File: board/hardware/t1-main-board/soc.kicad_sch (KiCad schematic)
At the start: 0 parts

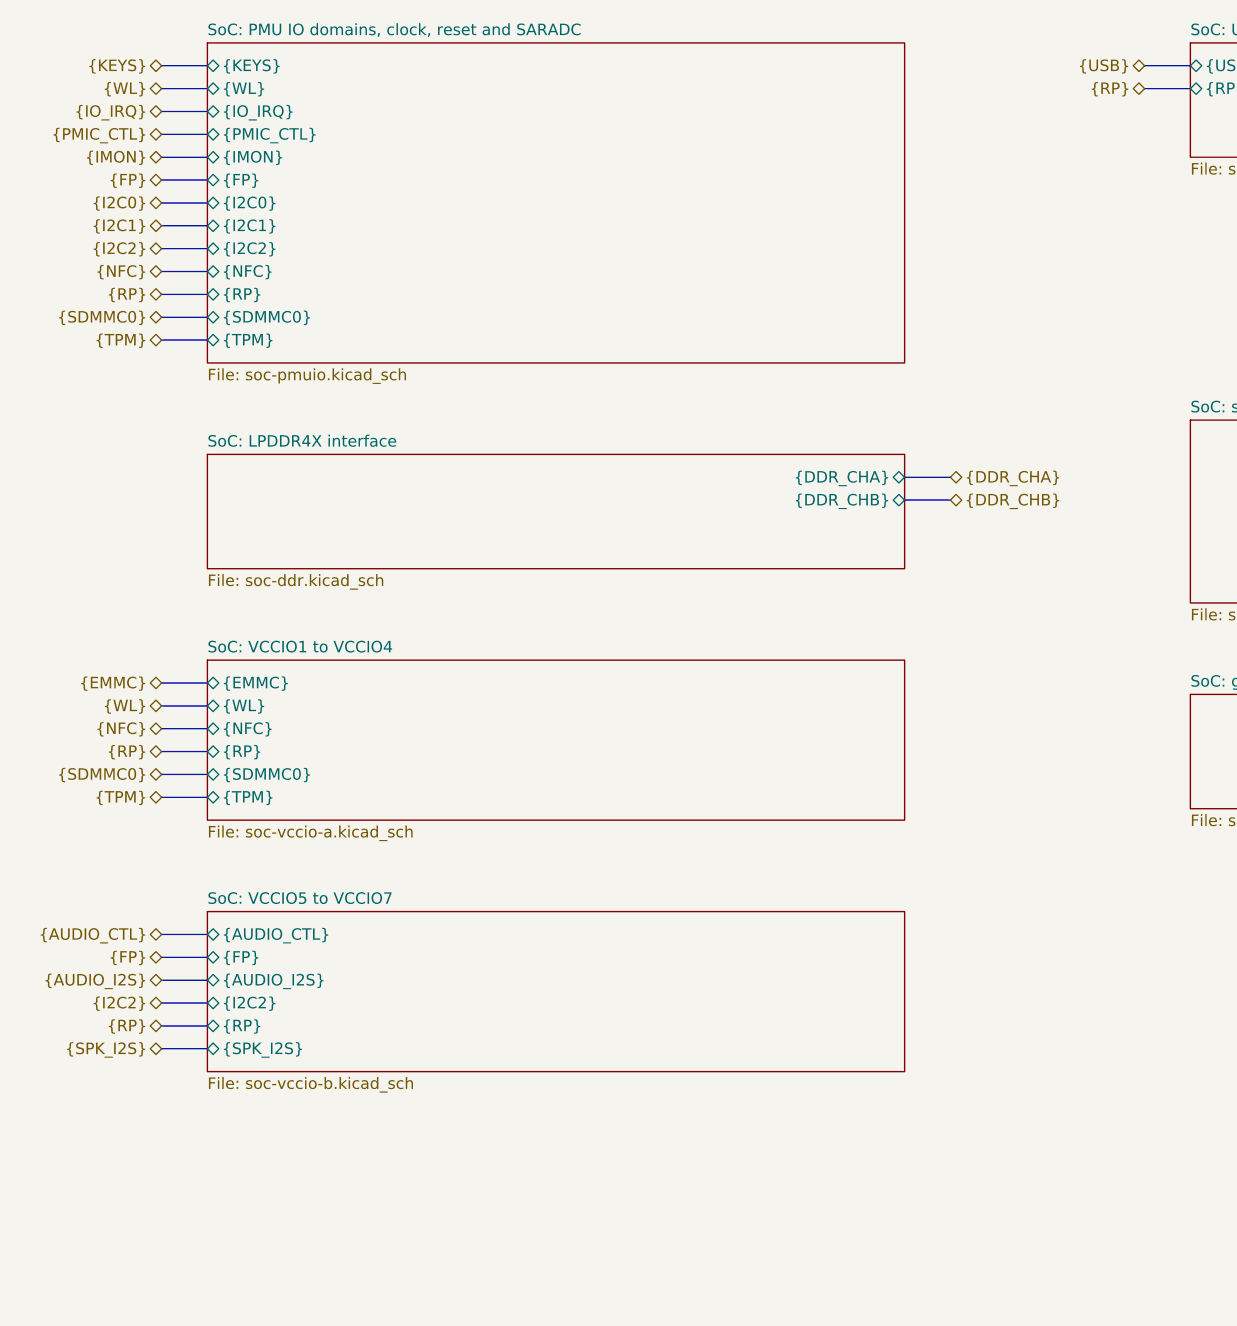
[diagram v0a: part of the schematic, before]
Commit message: Board: capture blk.debug
Debug UART2 (1.8 V) and I2S/DSD pads with ground pads, reset, PMIC and
power-key pads (PCB-T-09), a pad on every spare SoC GPIO whose pinout v1
row names one (the DEBUG bus, on the SoC's right edge), and a rail pad
for each power-tree rail no other sheet probes (PCB-T-02). Each DAC
sheet carries a pad on its MCLK. The spares pinout v1 leaves without a
pad now carry no-connect flags. On the root, facing sheet pins are
joined directly only where the route meets no other symbol.

Co-Authored-By: Claude Opus 5.5 <noreply@anthropic.com>
Claude-Session: https://claude.ai/code/session_01Ei262h3TpgY9vyfNLMi5Mn
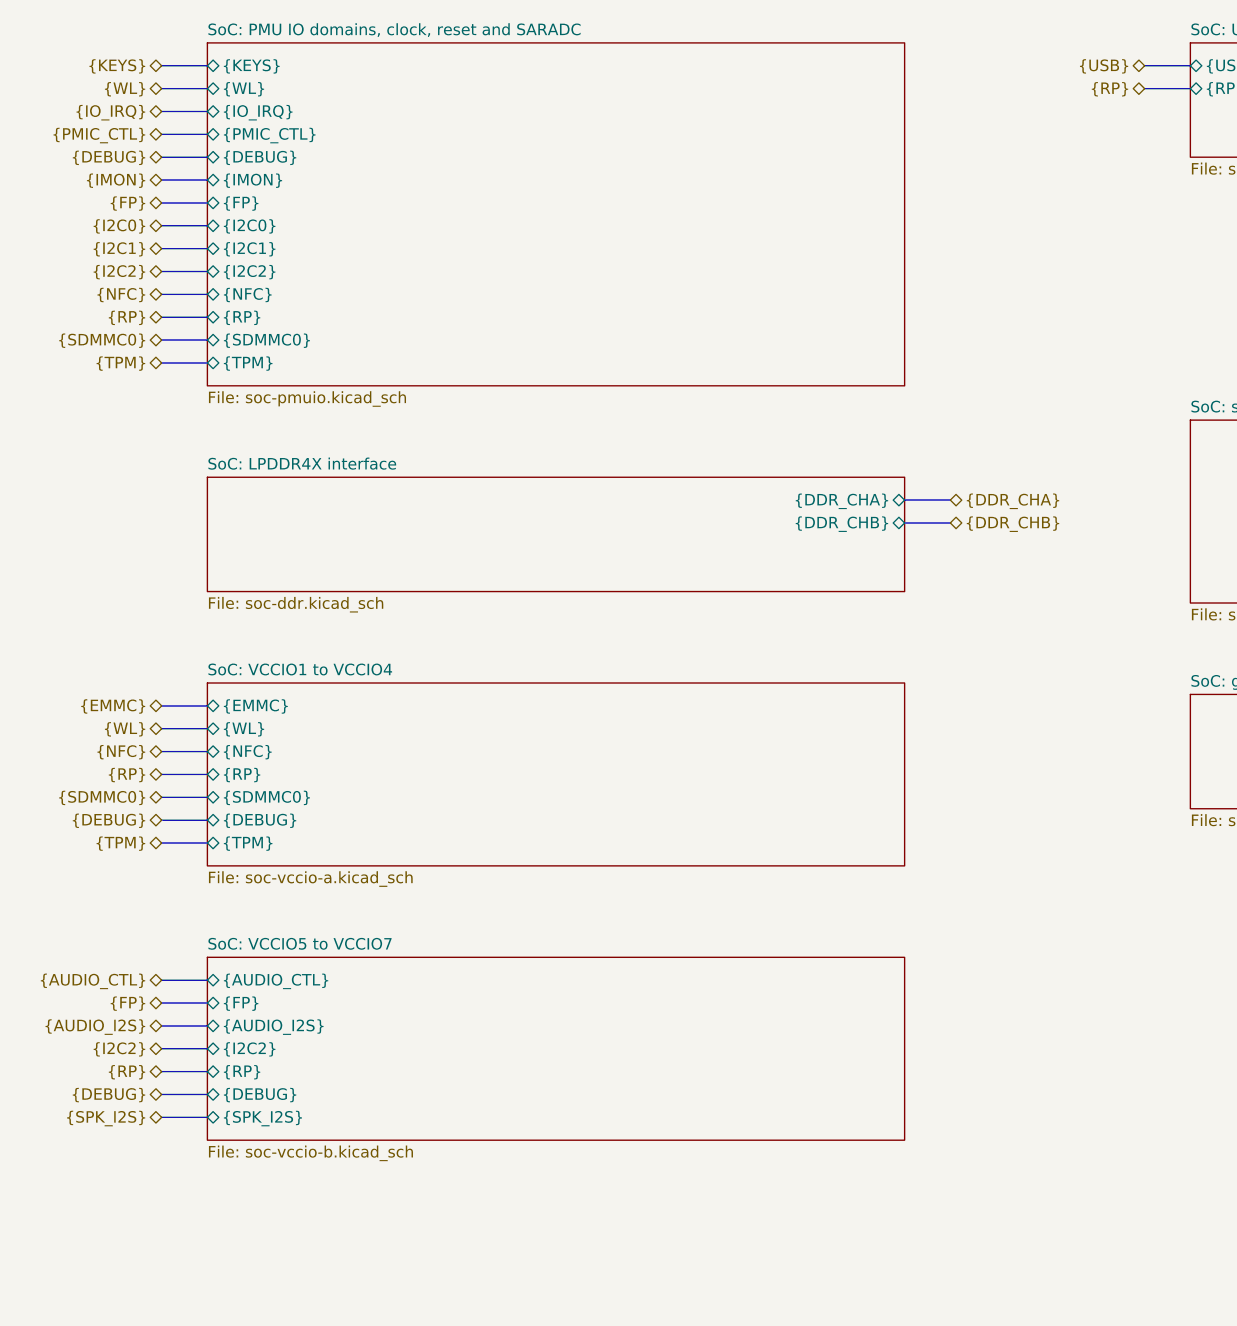
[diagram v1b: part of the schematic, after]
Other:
- sheet SoC: PMU IO domains, clock, reset and SARADC ports: added {DEBUG}; removed none
- sheet SoC: VCCIO1 to VCCIO4 ports: added {DEBUG}; removed none
- sheet SoC: VCCIO5 to VCCIO7 ports: added {DEBUG}; removed none

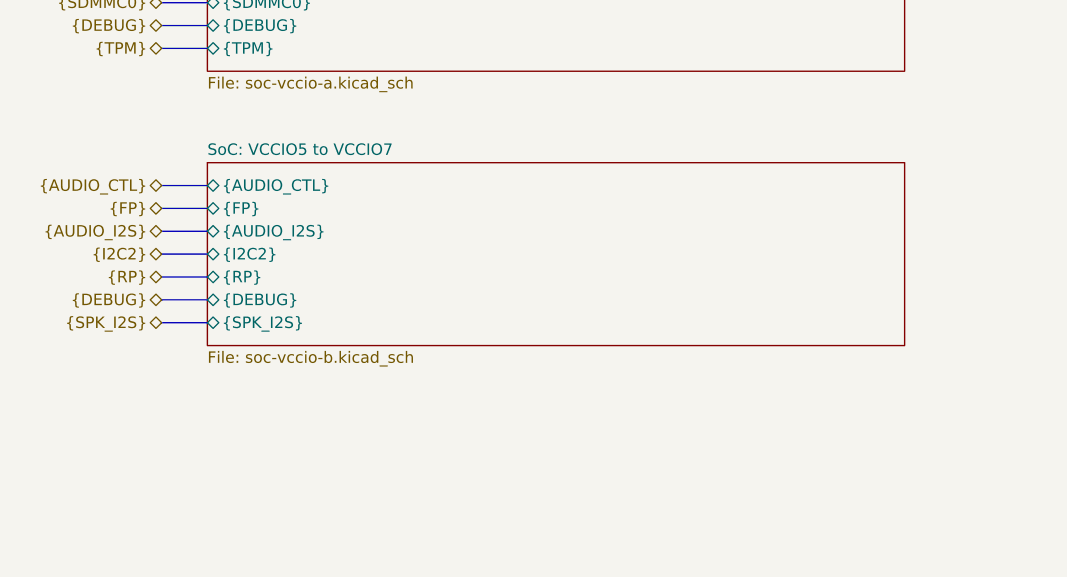
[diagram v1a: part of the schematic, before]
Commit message: Board: capture blk.mic-ambient and links #34, #35
IM73D122 on PDM CLK1 and SDI1 (BOM v1 line 34, pinout v1 AK2 and 1P2),
LR to ground, 22 Ω clock series, VDD from MIC_1V8 through link #35.
Link #34 on blk.mic-main makes the faceplate branch the rail MIC_1V8_FP
for contact 40 (power tree §4.12, G10). kicad-lib moves to e46bda4 for
the IM73D122, TPS3808G01, SN74LVC1G58 and BAT54 parts.

Co-Authored-By: Claude Opus 5.5 <noreply@anthropic.com>
Claude-Session: https://claude.ai/code/session_01Ei262h3TpgY9vyfNLMi5Mn
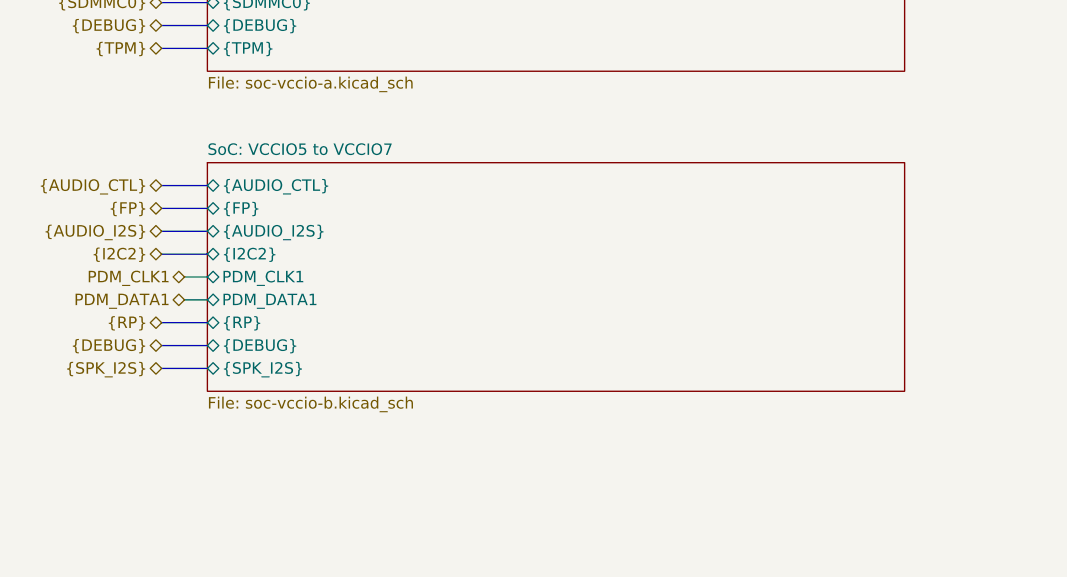
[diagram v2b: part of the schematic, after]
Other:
- sheet SoC: VCCIO5 to VCCIO7 ports: added PDM_CLK1, PDM_DATA1; removed none
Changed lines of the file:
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@@
   (instances (project "t1-main-board" (path "/7746052e-d7f9-59ad-ba73-bd2b74439529/8302eaa7-1fc9-5a34-8a84-8a9171d22bdf" (page "16"))))
 )
-(sheet (at 41.91 132.08) (size 77.47 20.32) (exclude_from_sim no) (in_bom yes) (on_board yes) (dnp no) (fields_autoplaced yes) (stroke (width 0.1524) (type solid)) (fill (color 0 0 0 0.0000))
+(sheet (at 41.91 132.08) (size 77.47 25.4) (exclude_from_sim no) (in_bom yes) (on_board yes) (dnp no) (fields_autoplaced yes) (stroke (width 0.1524) (type solid)) (fill (color 0 0 0 0.0000))
   (property "Sheetname" "SoC: VCCIO5 to VCCIO7" (at 41.91 131.368 0) (effects (font (size 1.27 1.27)) (justify left bottom)))
-  (property "Sheetfile" "soc-vccio-b.kicad_sch" (at 41.91 152.988 0) (effects (font (size 1.27 1.27)) (justify left top)))
-  (property "Block" "blk.soc-vccio-b" (at 41.91 155.528 0) (effects (font (size 1.27 1.27)) (justify left top)) (hide yes))
+  (property "Sheetfile" "soc-vccio-b.kicad_sch" (at 41.91 158.068 0) (effects (font (size 1.27 1.27)) (justify left top)))
+  (property "Block" "blk.soc-vccio-b" (at 41.91 160.608 0) (effects (font (size 1.27 1.27)) (justify left top)) (hide yes))
   (pin "{AUDIO_CTL}" bidirectional (at 41.91 134.62 180) (effects (font (size 1.27 1.27)) (justify left)))
   (pin "{FP}" bidirectional (at 41.91 137.16 180) (effects (font (size 1.27 1.27)) (justify left)))
   (pin "{AUDIO_I2S}" bidirectional (at 41.91 139.7 180) (effects (font (size 1.27 1.27)) (justify left)))
   (pin "{I2C2}" bidirectional (at 41.91 142.24 180) (effects (font (size 1.27 1.27)) (justify left)))
-  (pin "{RP}" bidirectional (at 41.91 144.78 180) (effects (font (size 1.27 1.27)) (justify left)))
-  (pin "{DEBUG}" bidirectional (at 41.91 147.32 180) (effects (font (size 1.27 1.27)) (justify left)))
-  (pin "{SPK_I2S}" bidirectional (at 41.91 149.86 180) (effects (font (size 1.27 1.27)) (justify left)))
+  (pin "PDM_CLK1" bidirectional (at 41.91 144.78 180) (effects (font (size 1.27 1.27)) (justify left)))
+  (pin "PDM_DATA1" bidirectional (at 41.91 147.32 180) (effects (font (size 1.27 1.27)) (justify left)))
+  (pin "{RP}" bidirectional (at 41.91 149.86 180) (effects (font (size 1.27 1.27)) (justify left)))
+  (pin "{DEBUG}" bidirectional (at 41.91 152.4 180) (effects (font (size 1.27 1.27)) (justify left)))
+  (pin "{SPK_I2S}" bidirectional (at 41.91 154.94 180) (effects (font (size 1.27 1.27)) (justify left)))
   (instances (project "t1-main-board" (path "/7746052e-d7f9-59ad-ba73-bd2b74439529/8302eaa7-1fc9-5a34-8a84-8a9171d22bdf" (page "17"))))
 )
@@
 (bus (pts (xy 41.91 116.84) (xy 36.83 116.84)) (stroke (width 0) (type default)))
 (hierarchical_label "{DEBUG}" (shape bidirectional) (at 36.83 116.84 180) (effects (font (size 1.27 1.27)) (justify right)))
-(bus (pts (xy 41.91 147.32) (xy 36.83 147.32)) (stroke (width 0) (type default)))
-(hierarchical_label "{DEBUG}" (shape bidirectional) (at 36.83 147.32 180) (effects (font (size 1.27 1.27)) (justify right)))
+(bus (pts (xy 41.91 152.4) (xy 36.83 152.4)) (stroke (width 0) (type default)))
+(hierarchical_label "{DEBUG}" (shape bidirectional) (at 36.83 152.4 180) (effects (font (size 1.27 1.27)) (justify right)))
 (bus (pts (xy 41.91 45.72) (xy 36.83 45.72)) (stroke (width 0) (type default)))
 (hierarchical_label "{IMON}" (shape bidirectional) (at 36.83 45.72 180) (effects (font (size 1.27 1.27)) (justify right)))
@@
 (bus (pts (xy 41.91 111.76) (xy 36.83 111.76)) (stroke (width 0) (type default)))
 (hierarchical_label "{RP}" (shape bidirectional) (at 36.83 111.76 180) (effects (font (size 1.27 1.27)) (justify right)))
-(bus (pts (xy 41.91 144.78) (xy 36.83 144.78)) (stroke (width 0) (type default)))
-(hierarchical_label "{RP}" (shape bidirectional) (at 36.83 144.78 180) (effects (font (size 1.27 1.27)) (justify right)))
+(bus (pts (xy 41.91 149.86) (xy 36.83 149.86)) (stroke (width 0) (type default)))
+(hierarchical_label "{RP}" (shape bidirectional) (at 36.83 149.86 180) (effects (font (size 1.27 1.27)) (justify right)))
 (bus (pts (xy 151.13 35.56) (xy 146.05 35.56)) (stroke (width 0) (type default)))
 (hierarchical_label "{RP}" (shape bidirectional) (at 146.05 35.56 180) (effects (font (size 1.27 1.27)) (justify right)))
@@
 (bus (pts (xy 41.91 139.7) (xy 36.83 139.7)) (stroke (width 0) (type default)))
 (hierarchical_label "{AUDIO_I2S}" (shape bidirectional) (at 36.83 139.7 180) (effects (font (size 1.27 1.27)) (justify right)))
-(bus (pts (xy 41.91 149.86) (xy 36.83 149.86)) (stroke (width 0) (type default)))
-(hierarchical_label "{SPK_I2S}" (shape bidirectional) (at 36.83 149.86 180) (effects (font (size 1.27 1.27)) (justify right)))
+(wire (pts (xy 41.91 144.78) (xy 39.37 144.78)) (stroke (width 0) (type default)))
+(hierarchical_label "PDM_CLK1" (shape bidirectional) (at 39.37 144.78 180) (effects (font (size 1.27 1.27)) (justify right)))
+(wire (pts (xy 41.91 147.32) (xy 39.37 147.32)) (stroke (width 0) (type default)))
+(hierarchical_label "PDM_DATA1" (shape bidirectional) (at 39.37 147.32 180) (effects (font (size 1.27 1.27)) (justify right)))
+(bus (pts (xy 41.91 154.94) (xy 36.83 154.94)) (stroke (width 0) (type default)))
+(hierarchical_label "{SPK_I2S}" (shape bidirectional) (at 36.83 154.94 180) (effects (font (size 1.27 1.27)) (justify right)))
 (bus (pts (xy 151.13 33.02) (xy 146.05 33.02)) (stroke (width 0) (type default)))
 (hierarchical_label "{USB}" (shape bidirectional) (at 146.05 33.02 180) (effects (font (size 1.27 1.27)) (justify right)))

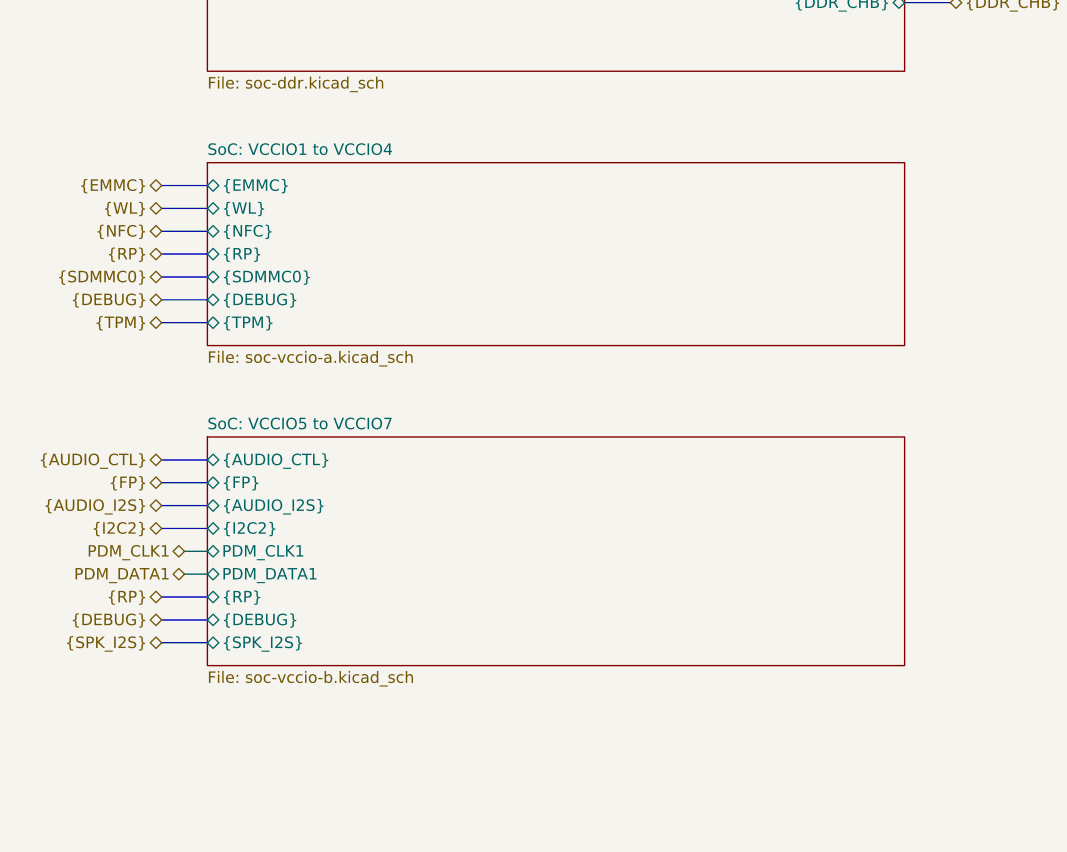
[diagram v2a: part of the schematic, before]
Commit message: NFC reader withdrawn from the board, every model (BRD-057)
Maintainer decision 2026-10-27, reason: board area. blk.nfc-reader (#42)
withdrawn: PN7160, front end, crystal, antenna contacts, NFC_VBAT switch
and link #18 removed (35 parts). BRD-057 reworded: NFC as the dynamic tag
only; blk.nfc-tag stays. Pinout v1: 1N20, A37, B38 become unconnected
spares, expander P05 a spare. BOM v1.18 item 7 (line 50: 5 switches,
lines 127-128 withdrawn), power tree v0.10, variant files, feature blocks.

Sheets after the removed one move up a page; references renumbered in
plan.py, parts.py and the specs (J6201 -> J6101 and others).

Placement v1.4: 990 parts placed, board need 96.9 % (99.1 % before),
factor 1.72; 243 capacitors within bound; DRC 0 errors; ERC 0 errors;
craft Q1 met; overlaps 0; pcb tests pass; STEP exported.

Co-Authored-By: Claude Opus 5.5 <noreply@anthropic.com>
Claude-Session: https://claude.ai/code/session_01Ei262h3TpgY9vyfNLMi5Mn
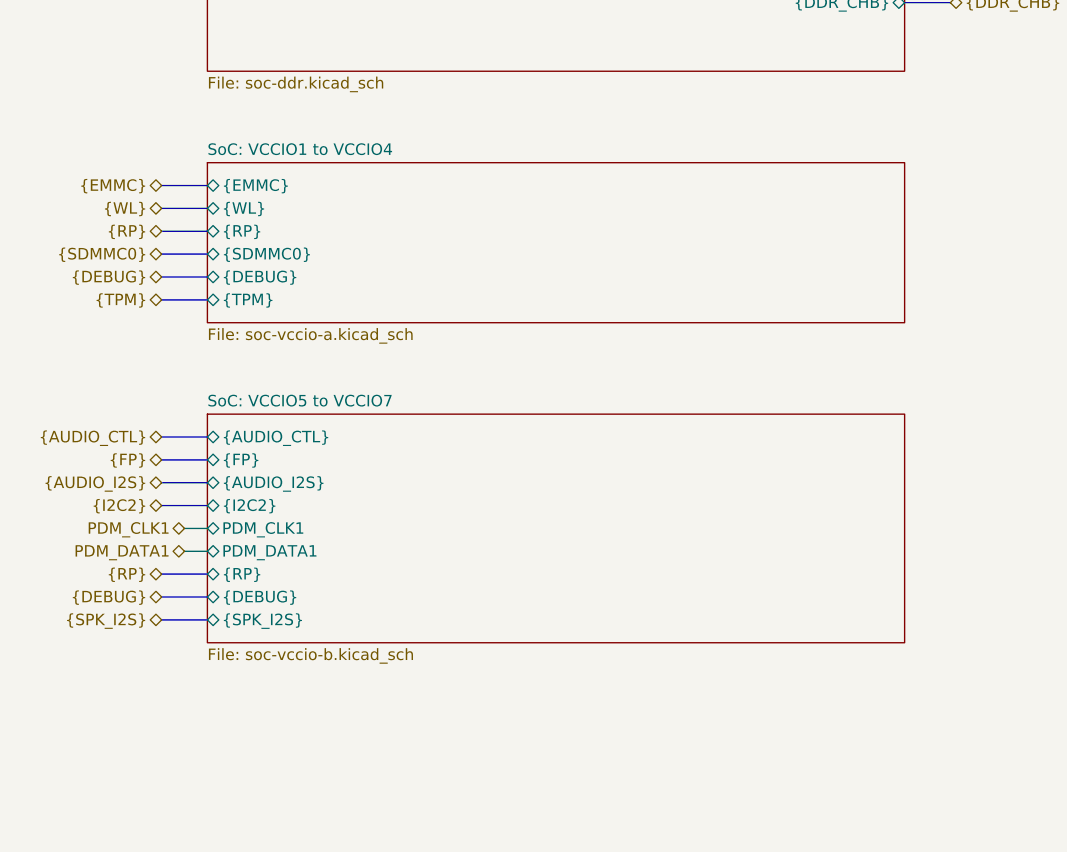
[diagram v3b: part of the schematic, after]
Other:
- sheet SoC: VCCIO1 to VCCIO4 ports: added none; removed {NFC}
